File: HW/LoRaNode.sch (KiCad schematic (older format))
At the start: 37 parts, among them J1 UART, J2 I2C, J3 SPI, J4 5V_IN, J5 BAT_IN, J6 SWD, J7 RS485, U1 STM32L071CBTx, U2 E22-900M22S, U3 MAX3483, X1 8MHz, X2 32.768KHz

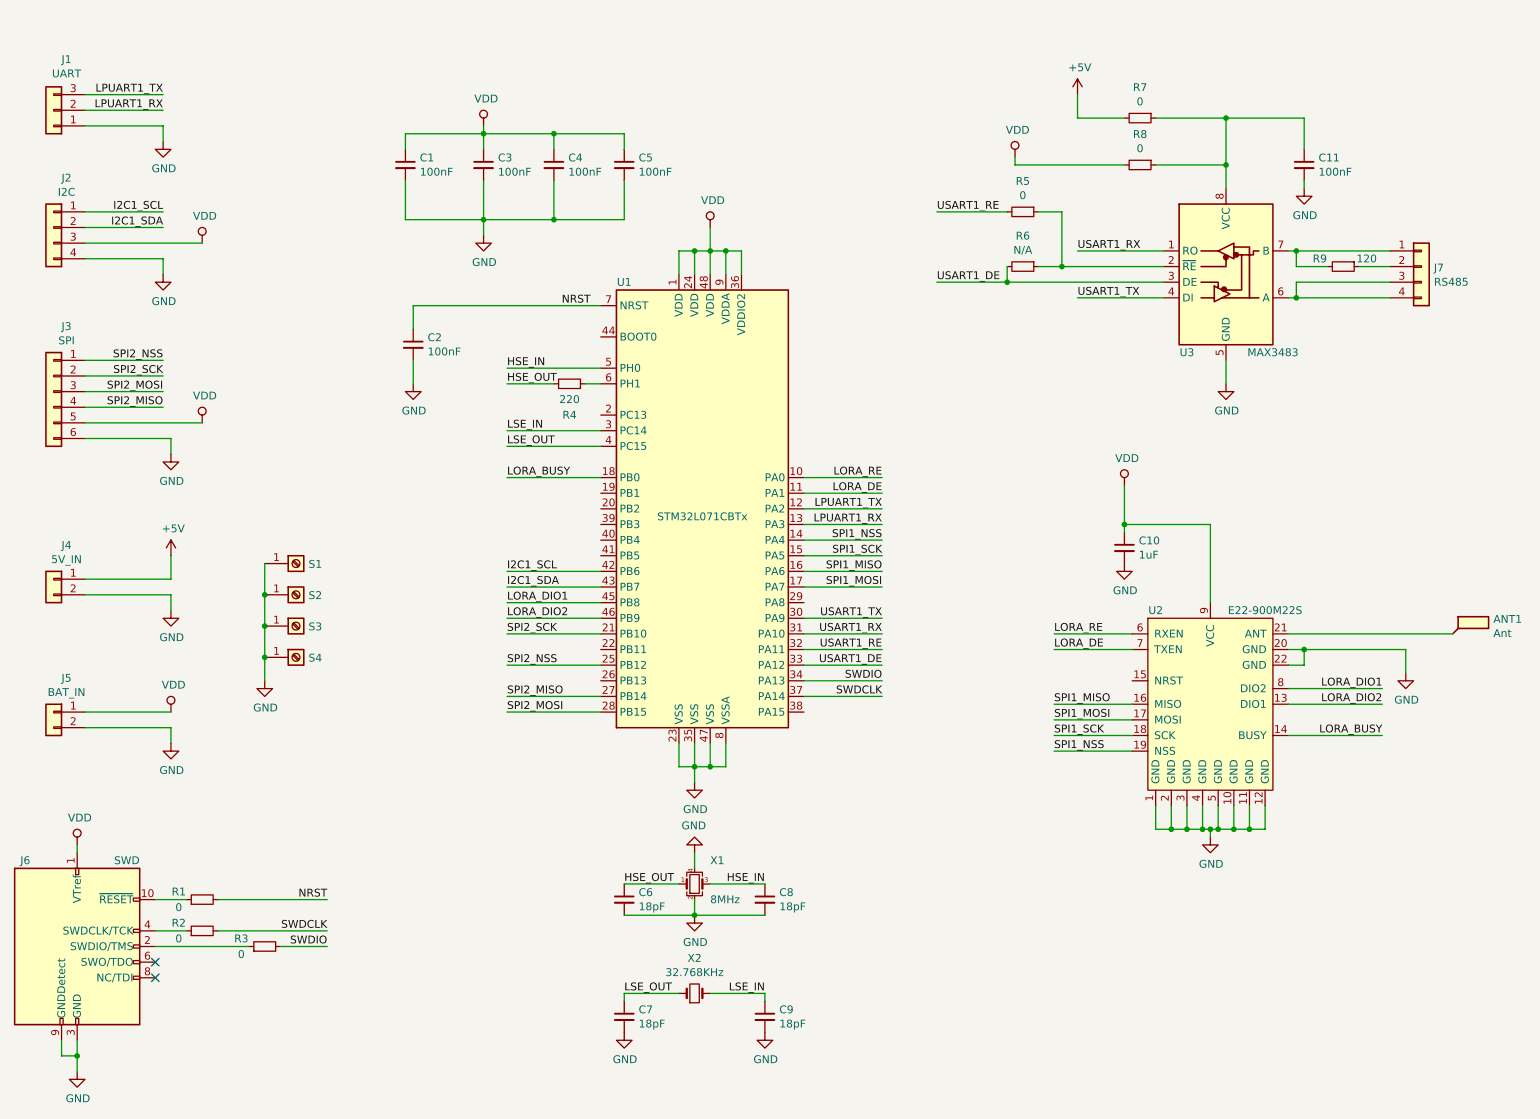
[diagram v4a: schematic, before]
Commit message: add lost decouple capacitor
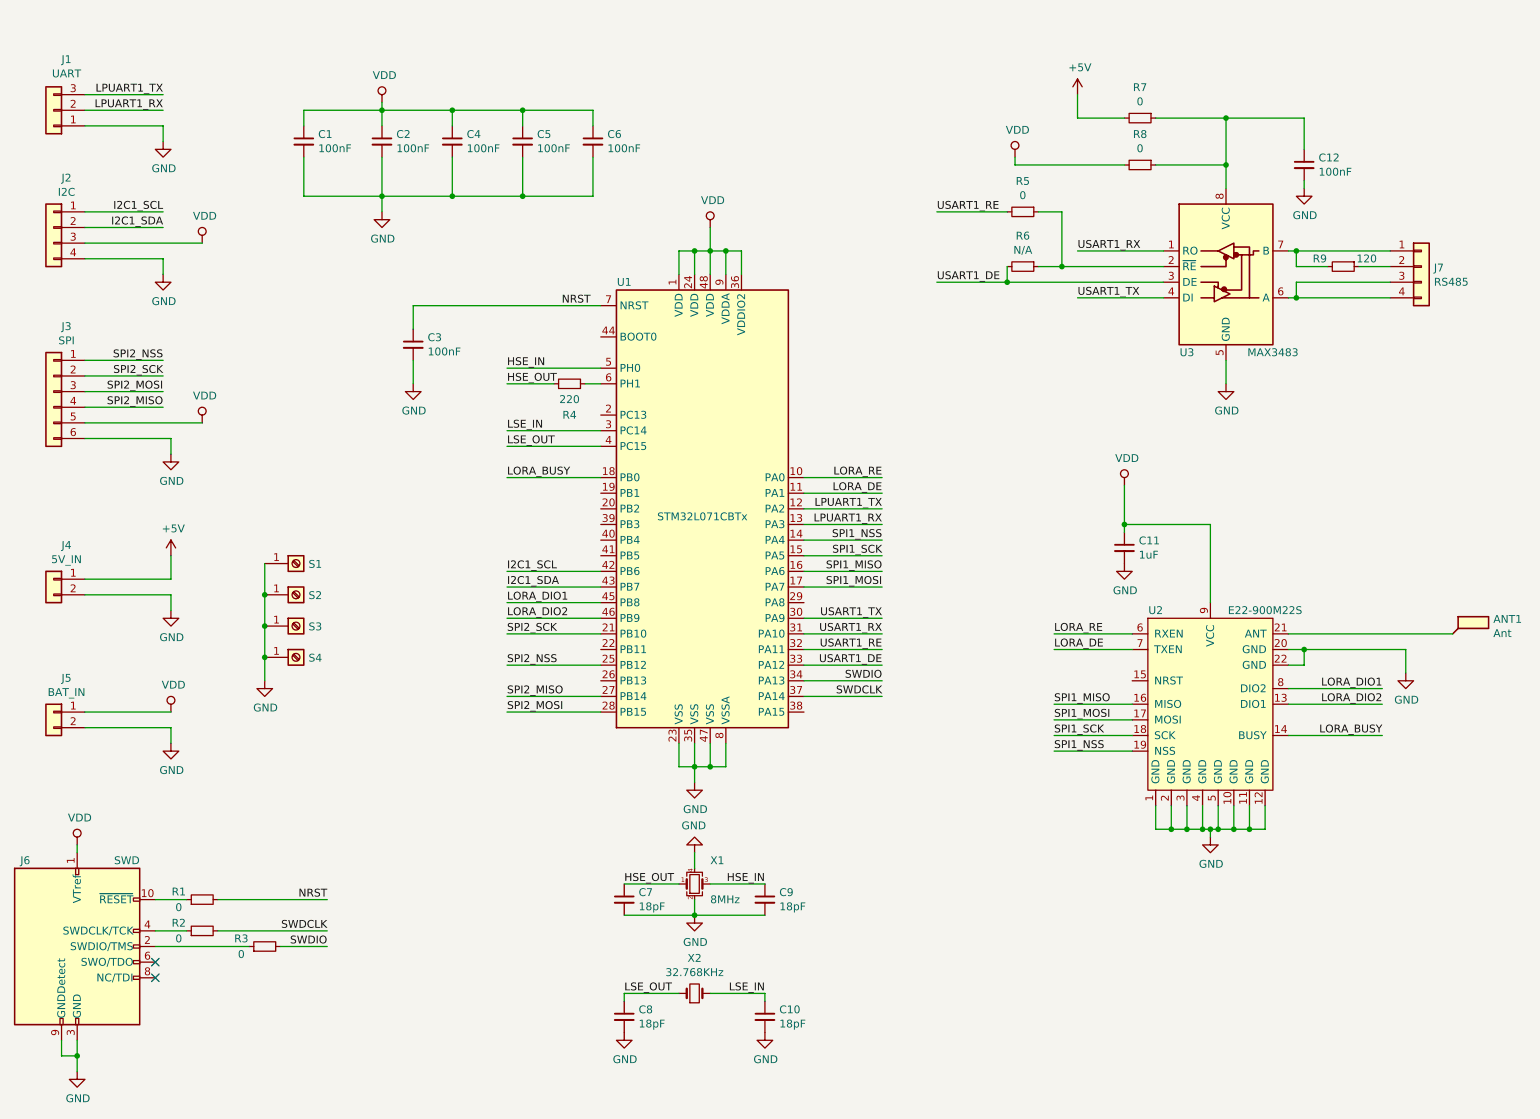
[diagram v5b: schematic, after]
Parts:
- added C6: 100nF, Capacitor_SMD:C_0402_1005Metric, symbol Device:C_Small
- renumbered C9 to C10, C10 to C11, C11 to C12, C3 to C2, C2 to C3, C6 to C7, C7 to C8, C8 to C9
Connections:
- net GND: now also C6.2
- net VDD: now also C6.1
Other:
- moved on the sheet: C1, C2, C4, C5
